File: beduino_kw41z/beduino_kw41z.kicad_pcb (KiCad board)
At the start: 2 copper layers, 66 x 18 mm, 57 parts, among them J1 USB_OTG, J2 Conn_01x07, J3 Conn_01x07, Q1 Q_PMOS_SGD, SW1 SW_Push, SW2 Reset, U1 TC1017, U2 LPC11U35FHI33-501, U3 TC1017, U4 Module_CONN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

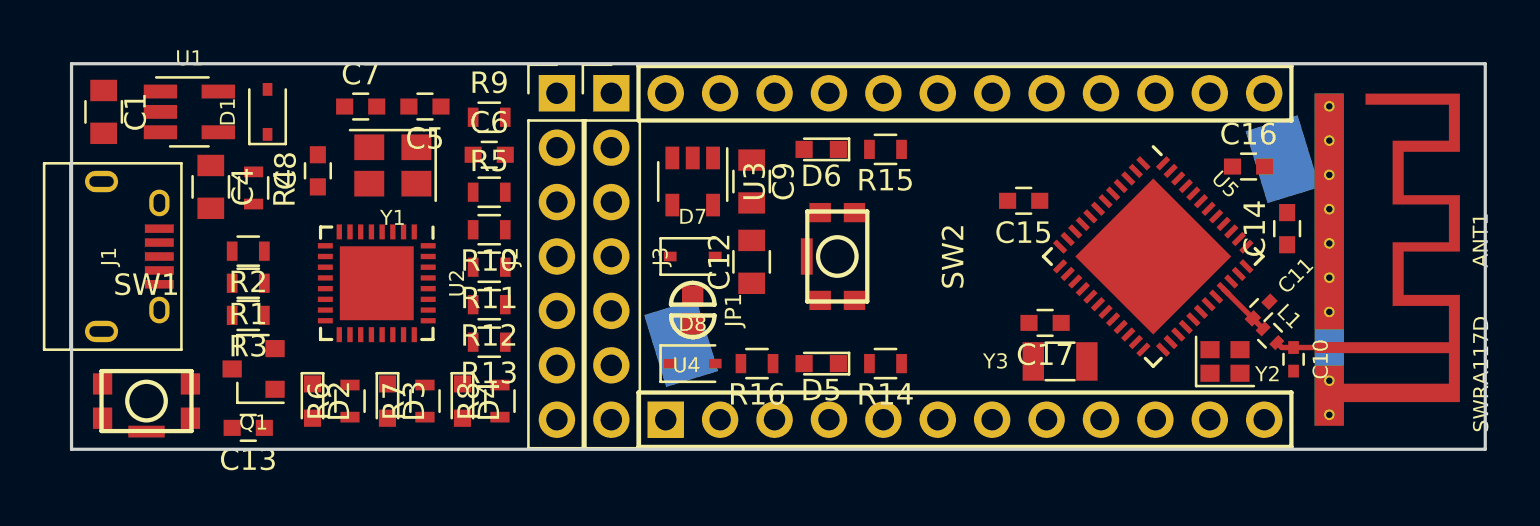
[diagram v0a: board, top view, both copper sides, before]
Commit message: Add some initial routing ideas.
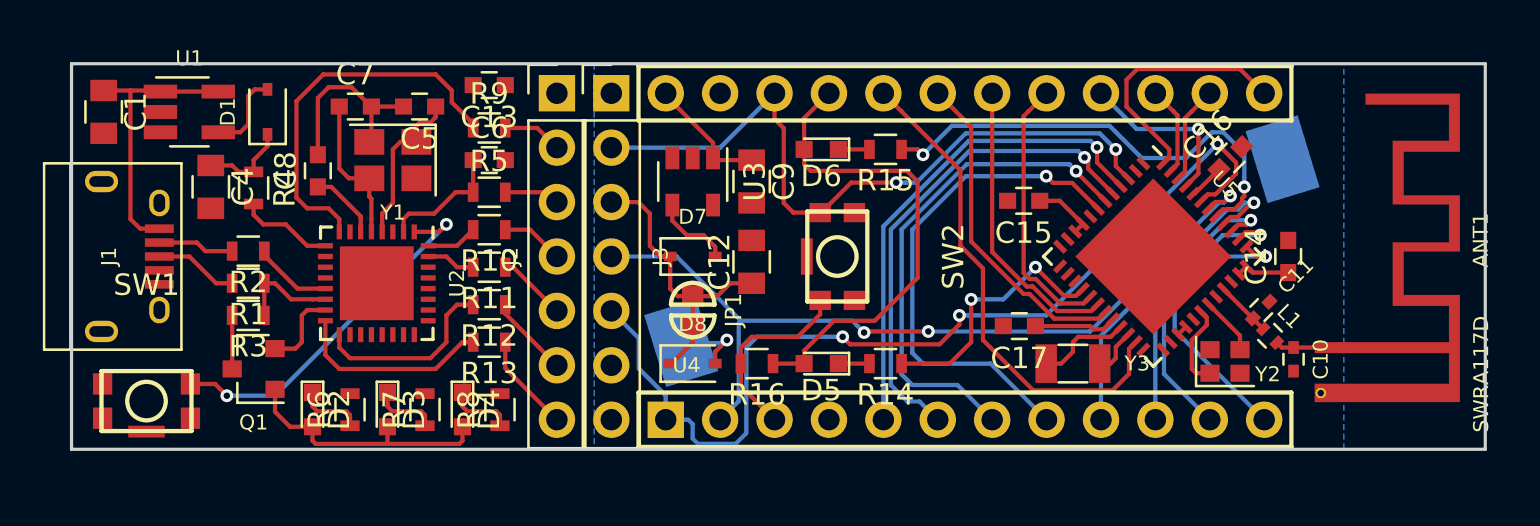
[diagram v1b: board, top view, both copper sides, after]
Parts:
- moved C13 19.6 mm to (75.5, 42.0)
- moved C14 1.30 mm to (112.8, 50.0)
- moved C17 1.21 mm to (100.2, 53.2)
- moved C16 0.94 mm to (110.1, 45.4), turned to 45 degrees
- moved Y3 0.61 mm to (102.8, 55.0), turned to 0 degrees
- moved R9 0.50 mm to (75.5, 44.0)
- moved D2 0.40 mm to (67.2, 57.1)
- moved D3 0.40 mm to (70.8, 57.1)
- moved D4 0.40 mm to (74.2, 57.1)
- moved R6 0.40 mm to (69.0, 57.1)
- moved R7 0.40 mm to (72.5, 57.1)
- moved R8 0.40 mm to (76.0, 57.1)
- moved C5 0.25 mm to (72.2, 43.0)
- moved C6 0.25 mm to (75.5, 45.5)
- moved C7 0.25 mm to (69.2, 43.0)
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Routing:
- net +3V3: track 0.00 -> 70.6 mm
- net /DIPDAP/TGT_TX: track 0.00 -> 48.6 mm, vias 0 -> 3
- net /DIPDAP/TGT_NRESET: track 0.00 -> 44.9 mm, vias 0 -> 2
- net /DIPDAP/TGT_RX: track 0.00 -> 42.2 mm, vias 0 -> 3
- net /KW41Z/D5: track 0.00 -> 23.6 mm, vias 0 -> 1
- net /KW41Z/D4: track 0.00 -> 23.4 mm, vias 0 -> 1
- net /KW41Z/A3: track 0.00 -> 23.2 mm
- net /KW41Z/D3: track 0.00 -> 23.0 mm, vias 0 -> 1
- net /KW41Z/D2: track 0.00 -> 23.0 mm, vias 0 -> 1
- net /KW41Z/LED_Green: track 0.00 -> 22.0 mm, vias 0 -> 2
- net Net-(R9-Pad2): track 0.00 -> 17.8 mm
- net Net-(SW1-Pad1): track 0.00 -> 17.1 mm, vias 0 -> 2
- net /KW41Z/A2: track 0.00 -> 15.5 mm
- net /KW41Z/D6: track 0.00 -> 15.5 mm, vias 0 -> 1
- net /KW41Z/D9: track 0.00 -> 13.7 mm, vias 0 -> 1
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- added copper zone on B.Cu, net GND
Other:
- net class Default: clearance 0.2 -> 0.15; trace_width 0.25 -> 0.2; via_dia 0.8 -> 0.6; via_drill 0.4 -> 0.3
- rule trace_clearance: 0.2 -> 0.15
- rule trace_min: 0.2 -> 0.15

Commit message: Some more PCB design work.
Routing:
- net +3V3: track 70.6 -> 104.4 mm, vias 0 -> 2
- net Net-(R7-Pad2): track 0.00 -> 12.2 mm, vias 0 -> 2
- net Net-(R6-Pad2): track 0.00 -> 10.5 mm, vias 0 -> 2
- net Net-(R8-Pad2): track 0.00 -> 8.11 mm, vias 0 -> 2
- net Net-(SW1-Pad1): track 17.1 -> 23.9 mm, vias 2 -> 3
- net GND: track 8.92 -> 13.4 mm
- net /KW41Z/A0: track 12.7 -> 14.3 mm
- net /KW41Z/A1: track 13.6 -> 14.3 mm

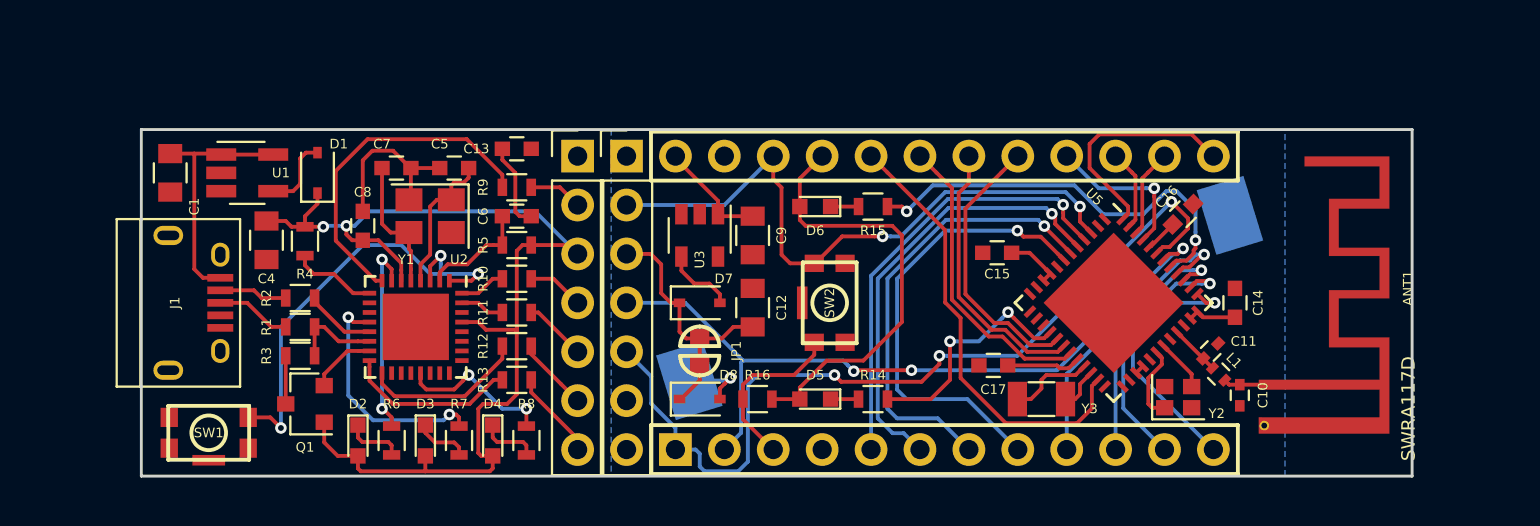
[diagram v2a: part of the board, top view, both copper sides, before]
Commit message: Finished routing. Needs checking.
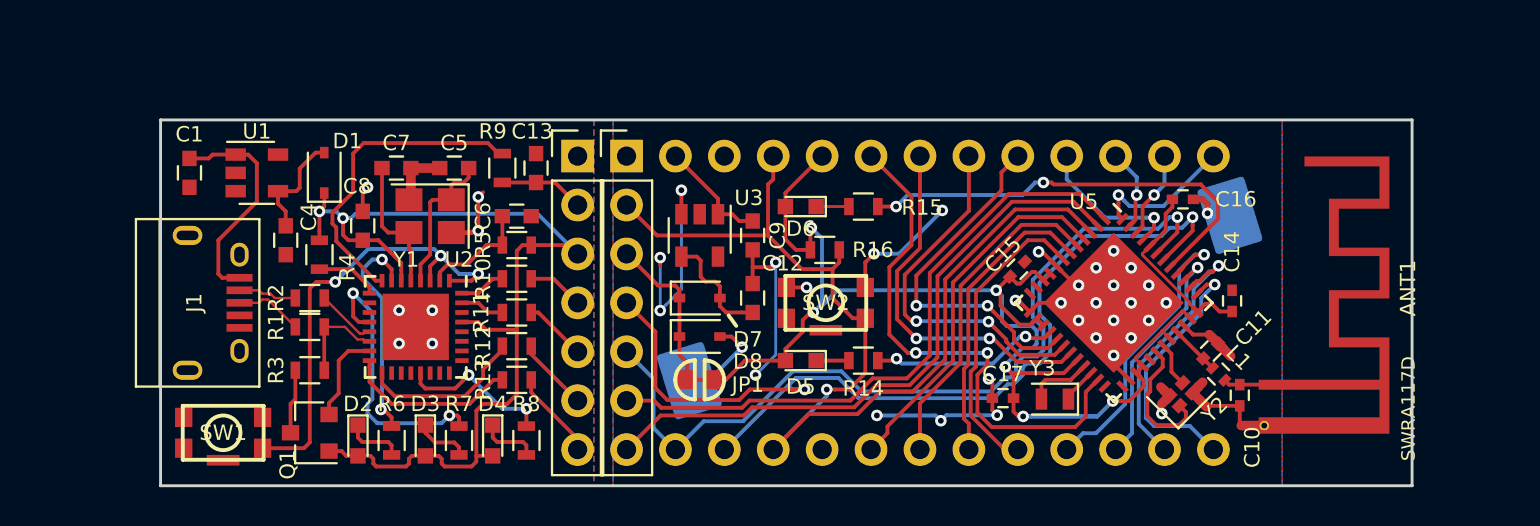
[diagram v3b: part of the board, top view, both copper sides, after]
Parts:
- C1, C12, C4, C9: footprint Capacitors_SMD:C_0805 -> Capacitors_SMD:C_0603
- C14, C15, C16, C17: footprint Capacitors_SMD:C_0603 -> Capacitors_SMD:C_0402
- U1: footprint TO_SOT_Packages_SMD:SOT-23-5_HandSoldering -> TO_SOT_Packages_SMD:SOT-23-5
- Y3: footprint Crystals:Crystal_SMD_3215-2pin_3.2x1.5mm -> Crystals:Crystal_SMD_2012-2pin_2.0x1.2mm
- moved R16 8.50 mm to (91.5, 47.2), turned to 0 degrees
- moved D8 3.25 mm to (85.0, 51.8)
- moved D5 2.14 mm to (90.2, 53.0)
- moved R14 2.06 mm to (93.5, 53.0)
- moved C17 1.77 mm to (100.8, 55.0)
- moved Q1 1.52 mm to (64.8, 56.8)
- moved JP1 1.50 mm to (85.0, 54.0), turned to 180 degrees
- moved C13 1.41 mm to (76.5, 43.0), turned to 90 degrees
- moved C15 1.35 mm to (101.5, 48.2), turned to 45 degrees
- moved R9 1.25 mm to (74.8, 43.0), turned to 90 degrees
- moved R4 1.03 mm to (65.2, 47.5)
- moved C1 1.00 mm to (58.5, 43.2)
- moved C4 1.00 mm to (63.5, 46.8)
- moved J1 1.00 mm to (59.8, 50.0)
- moved R3 0.90 mm to (64.8, 53.5)
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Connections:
- net Net-(J1-Pad2) renamed /DIPDAP/USB_N
- net Net-(J1-Pad3) renamed /DIPDAP/USB_P
- net Net-(R1-Pad1) renamed /DIPDAP/USB_R_P
- net Net-(R2-Pad1) renamed /DIPDAP/USB_R_N
- C12 pad 1: +3V3 -> Net-(C12-Pad1)
- C4 pad 1: +3V3 -> Net-(C4-Pad1)
- D1 pad 2: Net-(D1-Pad2) -> Net-(C4-Pad1)
- D7 pad 2: Net-(D7-Pad2) -> Net-(C12-Pad1)
- SW1 pad 1: Net-(SW1-Pad1) -> GND
- SW1 pad 2: GND -> Net-(SW1-Pad2)
- U1 pad 4: Net-(D1-Pad2) -> Net-(C4-Pad1)
- U1 pad 5: VBUS -> (no net)
- U2 pad 1: Net-(SW1-Pad1) -> Net-(SW1-Pad2)
- U2 pad 3: Net-(SW1-Pad1) -> Net-(SW1-Pad2)
- U3 pad 4: Net-(D7-Pad2) -> Net-(C12-Pad1)
- U3 pad 5: VCC -> (no net)
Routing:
- net GND: track 13.4 -> 92.5 mm, vias 0 -> 39
- net +3V3: track 104.4 -> 139.7 mm, vias 2 -> 8
- net /DIPDAP/TGT_SWCLK: track 4.62 -> 37.4 mm
- net /DIPDAP/TGT_SWDIO: track 3.83 -> 36.5 mm
- net Net-(SW1-Pad1): track 23.9 -> 0.00 mm, vias 3 -> 0
- net Net-(SW1-Pad2): track 0.00 -> 23.9 mm, vias 0 -> 3
- net /DIPDAP/TGT_NRESET: track 44.9 -> 59.6 mm, vias 2 -> 1
- net /DIPDAP/TGT_RX: track 42.2 -> 53.3 mm, vias 3 -> 2
- net /KW41Z/D4: track 23.4 -> 15.5 mm, vias 1 -> 0
- net /KW41Z/D5: track 23.6 -> 15.8 mm, vias 1 -> 0
- net Net-(C12-Pad1): track 0.00 -> 6.00 mm
- net /KW41Z/D3: track 23.0 -> 17.2 mm, vias 1 -> 0
- net Net-(C4-Pad1): track 0.00 -> 5.53 mm
- net /KW41Z/A1: track 14.3 -> 19.0 mm, vias 0 -> 2
- net /KW41Z/A3: track 23.2 -> 27.8 mm, vias 0 -> 2
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- added copper zone on F.Cu, net GND
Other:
- board size 66 x 18 mm -> 65 x 19 mm
- net class Default: trace_width 0.2 -> 0.15
- rule via_min_size: 0.4 -> 0.6
